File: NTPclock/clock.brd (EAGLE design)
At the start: 115 x 85 mm, 28 parts, among them IC1 MAX7219CNG

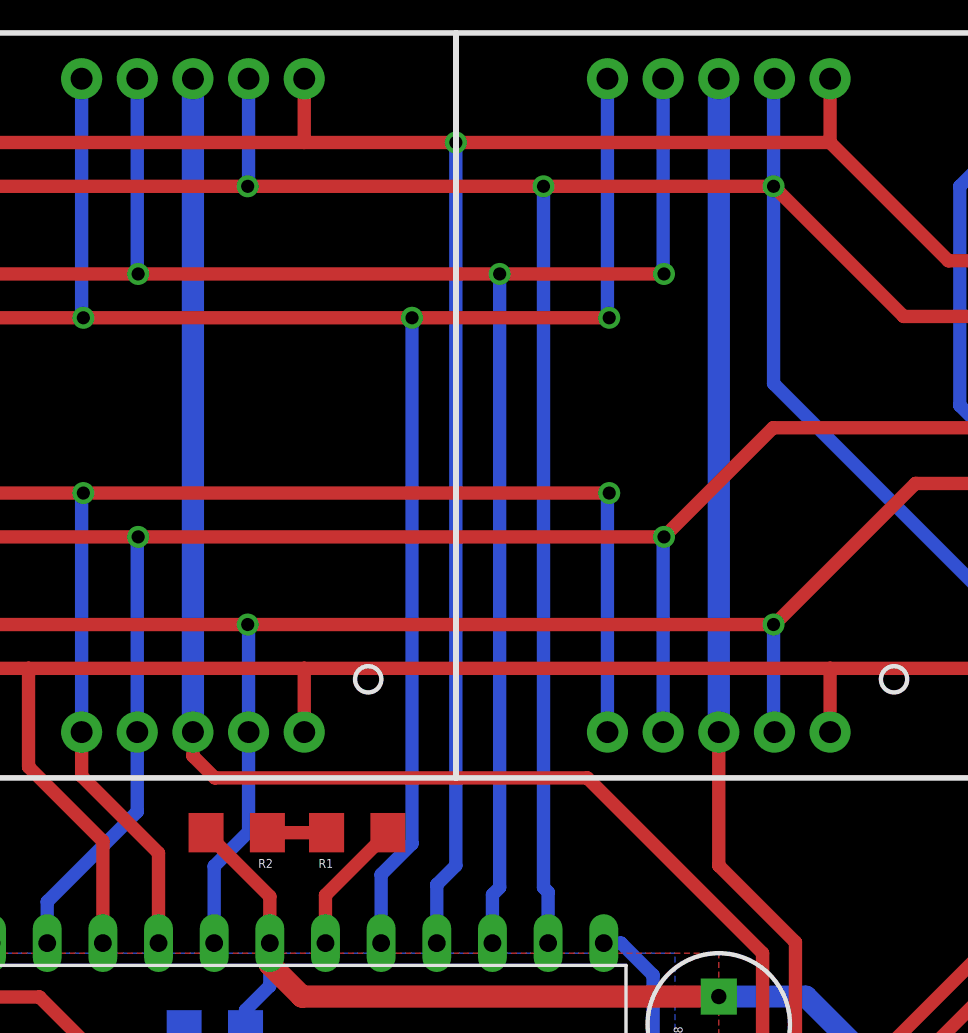
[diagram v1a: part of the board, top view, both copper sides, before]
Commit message: enable ground pour around lcds
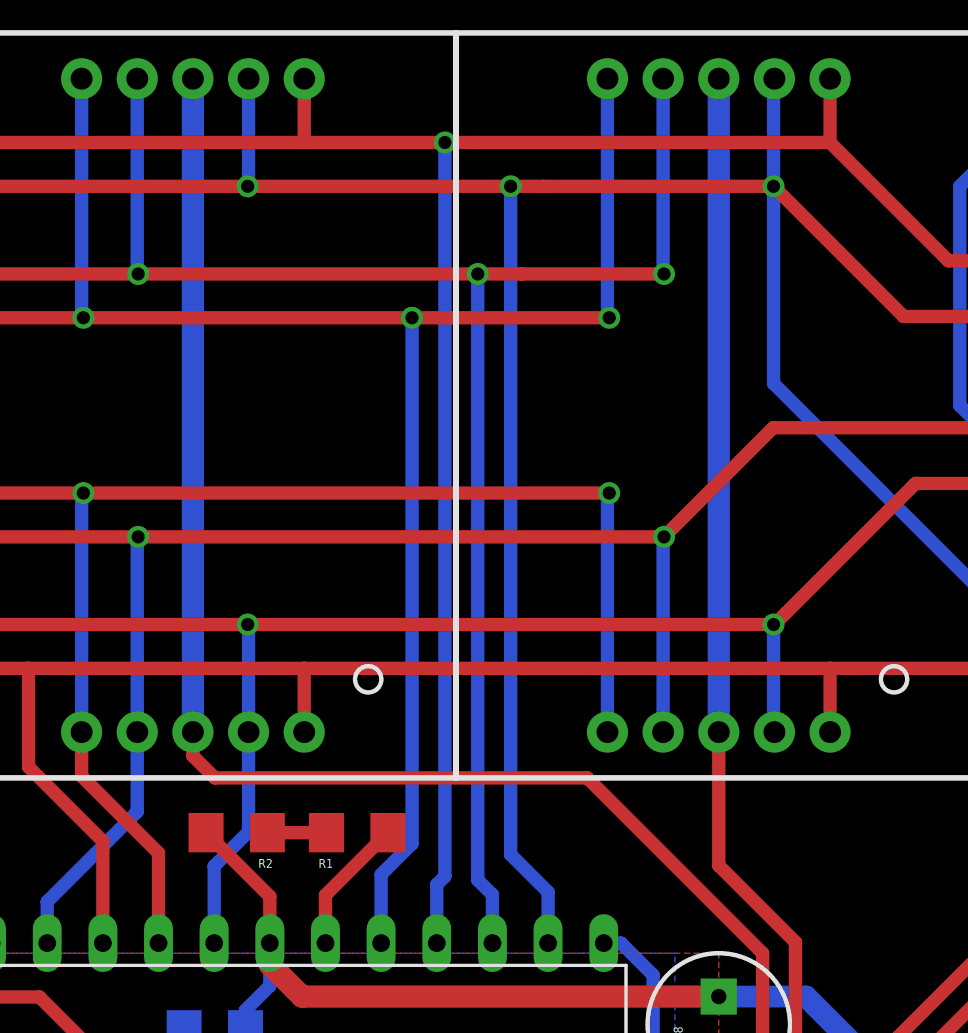
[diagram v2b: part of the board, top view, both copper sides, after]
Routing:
- net A: track 166.3 -> 166.9 mm
- removed copper zone on layer 1, net N$1
- removed copper zone on layer 16, net N$2
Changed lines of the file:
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@@
 <wire x1="91" y1="9.27" x2="60.13" y2="9.27" width="1" layer="1"/>
 <wire x1="60.13" y1="9.27" x2="60" y2="9.4" width="1" layer="1"/>
+<polygon width="0.6096" layer="16" isolate="0.6096">
+<vertex x="0" y="83"/>
+<vertex x="114" y="83"/>
+<vertex x="114" y="49"/>
+<vertex x="0" y="49"/>
+</polygon>
+<polygon width="0.6096" layer="1" isolate="0.6096">
+<vertex x="0" y="83"/>
+<vertex x="114" y="83"/>
+<vertex x="114" y="49"/>
+<vertex x="0" y="49"/>
+</polygon>
 </signal>
 <signal name="ISET">
@@
 <wire x1="19.45" y1="76" x2="38.5" y2="76" width="0.6096" layer="1"/>
 <wire x1="38.5" y1="76" x2="66.5" y2="76" width="0.6096" layer="1"/>
-<wire x1="66.5" y1="76" x2="80" y2="76" width="0.6096" layer="1"/>
+<wire x1="66.5" y1="76" x2="78.5" y2="76" width="0.6096" layer="1"/>
 <wire x1="80" y1="76" x2="90.5" y2="76" width="0.6096" layer="1"/>
 <wire x1="14.54" y1="80.91" x2="19.45" y2="76" width="0.6096" layer="1"/>
@@
 <via x="38.5" y="76" extent="1-16" drill="0.6" diameter="0.8"/>
 <wire x1="80.21" y1="41.46" x2="80.21" y2="43.79" width="0.6096" layer="16"/>
-<wire x1="80.21" y1="43.79" x2="80" y2="44" width="0.6096" layer="16"/>
-<wire x1="80" y1="44" x2="80" y2="76" width="0.6096" layer="16"/>
-<via x="80" y="76" extent="1-16" drill="0.6" diameter="0.8"/>
 <via x="90.5" y="76" extent="1-16" drill="0.6"/>
 <wire x1="90.5" y1="76" x2="90.5" y2="80.87" width="0.6096" layer="16"/>
@@
 <wire x1="102.19" y1="57.36" x2="100.14" y2="57.36" width="0.6096" layer="16"/>
 <wire x1="100.14" y1="57.36" x2="90.5" y2="67" width="0.6096" layer="16"/>
+<wire x1="80.21" y1="43.79" x2="78.5" y2="45.5" width="0.6096" layer="16"/>
+<wire x1="78.5" y1="45.5" x2="78.5" y2="76" width="0.6096" layer="16"/>
+<via x="78.5" y="76" extent="1-16" drill="0.6"/>
+<wire x1="78.5" y1="76" x2="80" y2="76" width="0.6096" layer="1"/>
 </signal>
 <signal name="B">
@@
 <wire x1="19.99" y1="78" x2="41.08" y2="78" width="0.6096" layer="1"/>
 <wire x1="41.08" y1="78" x2="69.08" y2="78" width="0.6096" layer="1"/>
-<wire x1="69.08" y1="78" x2="76" y2="78" width="0.6096" layer="1"/>
-<wire x1="76" y1="78" x2="93.08" y2="78" width="0.6096" layer="1"/>
+<wire x1="69.08" y1="78" x2="75.5" y2="78" width="0.6096" layer="1"/>
+<wire x1="77" y1="78" x2="93.08" y2="78" width="0.6096" layer="1"/>
 <wire x1="17.08" y1="80.91" x2="19.99" y2="78" width="0.6096" layer="1"/>
 <wire x1="41.08" y1="80.91" x2="41.08" y2="78" width="0.6096" layer="1"/>
@@
 <wire x1="93.08" y1="80.91" x2="93.08" y2="78" width="0.6096" layer="1"/>
 <wire x1="75.13" y1="41.46" x2="75.13" y2="44.13" width="0.6096" layer="16"/>
-<wire x1="75.13" y1="44.13" x2="76" y2="45" width="0.6096" layer="16"/>
-<wire x1="76" y1="45" x2="76" y2="78" width="0.6096" layer="16"/>
-<via x="76" y="78" extent="1-16" drill="0.6" diameter="0.8"/>
 <contactref element="BAR_GRAPH" pad="8"/>
 <contactref element="BAR_GRAPH" pad="3"/>
@@
 <wire x1="106" y1="62" x2="106" y2="71" width="0.6096" layer="1"/>
 <wire x1="106" y1="71" x2="104.4" y2="72.6" width="0.6096" layer="1"/>
+<wire x1="75.13" y1="44.13" x2="75.5" y2="44.5" width="0.6096" layer="16"/>
+<wire x1="75.5" y1="44.5" x2="75.5" y2="78" width="0.6096" layer="16"/>
+<via x="75.5" y="78" extent="1-16" drill="0.6"/>
+<wire x1="75.5" y1="78" x2="77" y2="78" width="0.6096" layer="1"/>
 </signal>
 <signal name="C">
@@
 <wire x1="33.5" y1="72" x2="48.73" y2="72" width="0.6096" layer="1"/>
 <wire x1="48.73" y1="72" x2="61.5" y2="72" width="0.6096" layer="1"/>
-<wire x1="61.5" y1="72" x2="78" y2="72" width="0.6096" layer="1"/>
-<wire x1="78" y1="72" x2="85.5" y2="72" width="0.6096" layer="1"/>
+<wire x1="61.5" y1="72" x2="77" y2="72" width="0.6096" layer="1"/>
+<wire x1="79" y1="72" x2="85.5" y2="72" width="0.6096" layer="1"/>
 <wire x1="85.46" y1="80.91" x2="85.46" y2="72" width="0.6096" layer="16"/>
 <wire x1="85.46" y1="72" x2="85.5" y2="72" width="0.6096" layer="16"/>
@@
 <wire x1="48.73" y1="74" x2="48.73" y2="72" width="0.6096" layer="1"/>
 <wire x1="77.67" y1="41.46" x2="77.67" y2="43.67" width="0.6096" layer="16"/>
-<wire x1="77.67" y1="43.67" x2="78" y2="44" width="0.6096" layer="16"/>
-<wire x1="78" y1="44" x2="78" y2="72" width="0.6096" layer="16"/>
-<via x="78" y="72" extent="1-16" drill="0.6" diameter="0.8"/>
+<wire x1="77.67" y1="43.67" x2="77" y2="44.34" width="0.6096" layer="16"/>
+<wire x1="77" y1="44.34" x2="77" y2="72" width="0.6096" layer="16"/>
+<via x="77" y="72" extent="1-16" drill="0.6"/>
+<wire x1="77" y1="72" x2="79" y2="72" width="0.6096" layer="1"/>
 </signal>
 <signal name="G">
@@
 <wire x1="20.6" y1="31" x2="16.4" y2="31" width="0.6096" layer="1"/>
 </signal>
-<signal name="N$1">
-<polygon width="0.6096" layer="1" pour="cutout">
-<vertex x="0" y="83"/>
-<vertex x="114" y="83"/>
-<vertex x="114" y="49"/>
-<vertex x="0" y="49"/>
-</polygon>
-</signal>
-<signal name="N$2">
-<polygon width="0.6096" layer="16" pour="cutout">
-<vertex x="0" y="83"/>
-<vertex x="114" y="83"/>
-<vertex x="114" y="49"/>
-<vertex x="0" y="49"/>
-</polygon>
-</signal>
 <signal name="N$3">

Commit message: Reorganize panel,
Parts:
- removed BUZ1: BUZZERPTH, SparkFun-Electromechanical:BUZZER-12MM
- removed J1: (no value), SparkFun-Connectors:1X02
- removed R4: 100Ω, SparkFun-Resistors:1206
- added BUTTONS: (no value), SparkFun-Connectors:MOLEX-1X6
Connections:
- removed net N$8: BUZ1.-, R4.1
- new net D3: BUTTONS.4, NODEMCU.V3.D3
- new net SD2: BUTTONS.5, NODEMCU.V3.SD2
- new net SD3: BUTTONS.6, NODEMCU.V3.SD3
- net D4: now also BUTTONS.3; no longer R4.2
- net D8: now also BUTTONS.2; no longer J1.1
- net GND: now also BUTTONS.1; no longer BUZ1.+, J1.2
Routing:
- net D3: track 0.00 -> 56.5 mm
- net SD2: track 0.00 -> 53.0 mm
- net SD3: track 0.00 -> 53.0 mm
- net GND: track 152.8 -> 121.3 mm
- net D8: track 23.2 -> 43.8 mm
- net D4: track 47.0 -> 56.5 mm
- net DIGIT7: track 63.8 -> 69.6 mm
- net N$8: track 5.43 -> 0.00 mm
- net DIGIT3: track 82.4 -> 85.6 mm
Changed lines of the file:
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@@
 <rectangle x1="31" y1="1" x2="49" y2="2" layer="41"/>
 <rectangle x1="31" y1="1" x2="49" y2="2" layer="42"/>
-<rectangle x1="31" y1="5" x2="32" y2="6" layer="42"/>
 <text x="55" y="-8" size="1.778" layer="48">Joshua villwock</text>
 <wire x1="115" y1="0" x2="115" y2="17" width="0" layer="20"/>
@@
 <text x="30.25" y="43" size="1.778" layer="21" rot="R270">RX
 TX</text>
+<rectangle x1="41" y1="24" x2="42" y2="25" layer="41"/>
 </plain>
 <attributes>
@@
 <attribute name="VALUE" x="51.905" y="56.349" size="1.27" layer="27" ratio="10"/>
 </element>
-<element name="BUZ1" library="SparkFun-Electromechanical" package="BUZZER-12MM" value="BUZZERPTH" x="70" y="21"/>
-<element name="J1" library="SparkFun-Connectors" package="1X02" value="" x="53" y="24"/>
-<element name="R4" library="SparkFun-Resistors" package="1206" value="100Ω" x="62" y="21.25" rot="R270"/>
 <element name="FRAME1" library="SparkFun-Aesthetics" package="CREATIVE_COMMONS" value="FRAME-LETTER" x="24" y="-8"/>
 <element name="SERIAL" library="SparkFun-Connectors" package="1X02" value="" x="33.75" y="37.75" rot="R180"/>
+<element name="BUTTONS" library="SparkFun-Connectors" package="MOLEX-1X6" value="" x="75" y="19" rot="MR0"/>
 </elements>
 <signals>
@@
 <wire x1="62.43" y1="35.43" x2="62.43" y2="33.84" width="1.016" layer="1"/>
 <wire x1="75.13" y1="33.84" x2="75.13" y2="36.48" width="1.016" layer="1"/>
-<wire x1="46" y1="9" x2="44" y2="7" width="0.6096" layer="1"/>
-<wire x1="44" y1="7" x2="41.25" y2="4.25" width="0.6096" layer="1"/>
-<wire x1="41.25" y1="4.25" x2="41.25" y2="3.13" width="0.6096" layer="1"/>
 <wire x1="23.47" y1="25.99" x2="23.4" y2="26.06" width="0.6096" layer="1"/>
 <wire x1="23.4" y1="26.06" x2="23.4" y2="31" width="0.6096" layer="1"/>
@@
 <vertex x="-2" y="87"/>
 </polygon>
-<wire x1="31.09" y1="3.13" x2="31.09" y2="5" width="0.6096" layer="1"/>
-<wire x1="31.09" y1="5" x2="31.09" y2="5.09" width="0.6096" layer="1"/>
-<wire x1="31.09" y1="5.09" x2="33" y2="7" width="0.6096" layer="1"/>
-<wire x1="33" y1="7" x2="44" y2="7" width="0.6096" layer="1"/>
-<wire x1="10.77" y1="3.13" x2="10.77" y2="4.27" width="0.6096" layer="1"/>
-<wire x1="11.5" y1="5" x2="31.09" y2="5" width="0.6096" layer="1"/>
-<wire x1="10.77" y1="4.27" x2="11.5" y2="5" width="0.6096" layer="1"/>
-<contactref element="J1" pad="2"/>
-<contactref element="BUZ1" pad="+"/>
 <wire x1="63.6" y1="37.5" x2="63.6" y2="36.6" width="0.6096" layer="16"/>
 <wire x1="63.6" y1="36.6" x2="62.43" y2="35.43" width="0.6096" layer="16"/>
@@
 <wire x1="60" y1="9.4" x2="54.63" y2="9.4" width="1" layer="1"/>
 <wire x1="54.63" y1="9.4" x2="54.5" y2="9.27" width="1" layer="1"/>
-<wire x1="46" y1="9" x2="54.23" y2="9" width="0.6096" layer="1"/>
-<wire x1="54.23" y1="9" x2="54.5" y2="9.27" width="0.6096" layer="1"/>
 <wire x1="91" y1="9.27" x2="60.13" y2="9.27" width="1" layer="1"/>
 <wire x1="60.13" y1="9.27" x2="60" y2="9.4" width="1" layer="1"/>
-<polygon width="0.6096" layer="16" isolate="0.6096">
-<vertex x="0" y="83"/>
-<vertex x="114" y="83"/>
-<vertex x="114" y="49"/>
-<vertex x="0" y="49"/>
-</polygon>
-<polygon width="0.6096" layer="1" isolate="0.6096">
-<vertex x="0" y="83"/>
-<vertex x="114" y="83"/>
-<vertex x="114" y="49"/>
-<vertex x="0" y="49"/>
-</polygon>
+<contactref element="BUTTONS" pad="1"/>
+<wire x1="10.77" y1="3.13" x2="12.64" y2="5" width="0.6096" layer="16"/>
+<wire x1="12.64" y1="5" x2="30" y2="5" width="0.6096" layer="16"/>
+<wire x1="30" y1="5" x2="31.09" y2="3.91" width="0.6096" layer="16"/>
+<wire x1="31.09" y1="3.91" x2="31.09" y2="3.13" width="0.6096" layer="16"/>
 </signal>
 <signal name="ISET">
@@
 <wire x1="76" y1="30" x2="79" y2="27" width="0.6096" layer="1"/>
 <wire x1="79" y1="27" x2="88" y2="27" width="0.6096" layer="1"/>
-<wire x1="88" y1="27" x2="107.5" y2="46.5" width="0.6096" layer="1"/>
-<wire x1="107.5" y1="66.5" x2="107.5" y2="46.5" width="0.6096" layer="1"/>
+<wire x1="107.5" y1="66.5" x2="107.5" y2="54" width="0.6096" layer="1"/>
+<wire x1="88" y1="27" x2="94.5" y2="33.5" width="0.6096" layer="1"/>
+<wire x1="94.5" y1="33.5" x2="94.5" y2="46.5" width="0.6096" layer="1"/>
+<wire x1="94.5" y1="46.5" x2="98.5" y2="50.5" width="0.6096" layer="1"/>
+<wire x1="98.5" y1="50.5" x2="104" y2="50.5" width="0.6096" layer="1"/>
+<wire x1="104" y1="50.5" x2="107.5" y2="54" width="0.6096" layer="1"/>
 </signal>
 <signal name="A">
@@
 <wire x1="76.5" y1="31.5" x2="79.5" y2="28.5" width="0.6096" layer="1"/>
 <wire x1="79.5" y1="28.5" x2="87.5" y2="28.5" width="0.6096" layer="1"/>
-<wire x1="87.5" y1="28.5" x2="105" y2="46" width="0.6096" layer="1"/>
-<via x="105" y="46" extent="1-16" drill="0.6" diameter="0.8"/>
-<wire x1="105" y1="46" x2="109.81" y2="50.81" width="0.6096" layer="16"/>
-<wire x1="109.81" y1="50.81" x2="109.81" y2="54.82" width="0.6096" layer="16"/>
+<wire x1="109.81" y1="54" x2="109.81" y2="54.82" width="0.6096" layer="16"/>
+<wire x1="87.5" y1="28.5" x2="93" y2="34" width="0.6096" layer="1"/>
+<wire x1="93" y1="34" x2="93" y2="47" width="0.6096" layer="1"/>
+<wire x1="93" y1="47" x2="98" y2="52" width="0.6096" layer="1"/>
+<wire x1="103" y1="52" x2="107.81" y2="52" width="0.6096" layer="16"/>
+<wire x1="107.81" y1="52" x2="109.81" y2="54" width="0.6096" layer="16"/>
+<wire x1="98" y1="52" x2="103" y2="52" width="0.6096" layer="1"/>
+<via x="103" y="52" extent="1-16" drill="0.6" diameter="0.8128"/>
 </signal>
 <signal name="DIGIT6">
@@
 <polygon width="0.6096" layer="16" pour="cutout">
 <vertex x="0" y="28"/>
-<vertex x="30" y="28"/>
-<vertex x="30" y="0"/>
+<vertex x="27" y="28"/>
+<vertex x="27" y="0"/>
 <vertex x="0" y="0"/>
 </polygon>
@@
 <polygon width="0.6096" layer="1" pour="cutout">
 <vertex x="0" y="28"/>
-<vertex x="30" y="28"/>
-<vertex x="30" y="0"/>
+<vertex x="27" y="28"/>
+<vertex x="27" y="0"/>
 <vertex x="0" y="0"/>
 </polygon>
@@
 <signal name="D4">
 <contactref element="NODEMCU.V3" pad="D4"/>
-<contactref element="R4" pad="2"/>
-<wire x1="18.39" y1="25.99" x2="18.39" y2="24.61" width="0.6096" layer="1"/>
-<wire x1="18.39" y1="24.61" x2="23" y2="20" width="0.6096" layer="1"/>
-<wire x1="23" y1="20" x2="61.85" y2="20" width="0.6096" layer="1"/>
-<wire x1="61.85" y1="20" x2="62" y2="19.85" width="0.6096" layer="1"/>
+<contactref element="BUTTONS" pad="3"/>
+<wire x1="18.39" y1="25.99" x2="24.38" y2="20" width="0.6096" layer="1"/>
+<wire x1="58" y1="20" x2="60.5" y2="22.5" width="0.6096" layer="1"/>
+<wire x1="60.5" y1="22.5" x2="66.42" y2="22.5" width="0.6096" layer="1"/>
+<wire x1="66.42" y1="22.5" x2="69.92" y2="19" width="0.6096" layer="1"/>
+<wire x1="24.38" y1="20" x2="58" y2="20" width="0.6096" layer="1"/>
 </signal>
 <signal name="D8">
 <contactref element="NODEMCU.V3" pad="D8"/>
-<contactref element="J1" pad="1"/>
-<wire x1="36.5" y1="21.5" x2="33.63" y2="24.37" width="0.6096" layer="1"/>
-<wire x1="33.63" y1="24.37" x2="33.63" y2="25.99" width="0.6096" layer="1"/>
-<wire x1="53" y1="24" x2="50.5" y2="21.5" width="0.6096" layer="1"/>
-<wire x1="50.5" y1="21.5" x2="36.5" y2="21.5" width="0.6096" layer="1"/>
-</signal>
-<signal name="N$8">
-<contactref element="R4" pad="1"/>
-<contactref element="BUZ1" pad="-"/>
-<wire x1="62" y1="22.65" x2="65.1" y2="22.65" width="0.6096" layer="1"/>
-<wire x1="65.1" y1="22.65" x2="66.75" y2="21" width="0.6096" layer="1"/>
+<contactref element="BUTTONS" pad="2"/>
+<wire x1="33.63" y1="25.99" x2="38.12" y2="21.5" width="0.6096" layer="1"/>
+<wire x1="57.5" y1="21.5" x2="60" y2="24" width="0.6096" layer="1"/>
+<wire x1="60" y1="24" x2="67.46" y2="24" width="0.6096" layer="1"/>
+<wire x1="67.46" y1="24" x2="72.46" y2="19" width="0.6096" layer="1"/>
+<wire x1="38.12" y1="21.5" x2="57.5" y2="21.5" width="0.6096" layer="1"/>
 </signal>
 <signal name="RX">
 <contactref element="NODEMCU.V3" pad="RX"/>
 <contactref element="SERIAL" pad="2"/>
-<wire x1="36.17" y1="25.99" x2="36.17" y2="29.83" width="0.4064" layer="1"/>
-<wire x1="36.17" y1="29.83" x2="31.21" y2="34.79" width="0.4064" layer="1"/>
-<wire x1="31.21" y1="34.79" x2="31.21" y2="37.75" width="0.4064" layer="1"/>
+<wire x1="36.17" y1="25.99" x2="36.17" y2="32.79" width="0.6096" layer="1"/>
+<wire x1="36.17" y1="32.79" x2="31.21" y2="37.75" width="0.6096" layer="1"/>
 </signal>
 <signal name="TX">
 <contactref element="NODEMCU.V3" pad="TX"/>
 <contactref element="SERIAL" pad="1"/>
-<wire x1="38.71" y1="25.99" x2="38.71" y2="29.29" width="0.4064" layer="1"/>
-<wire x1="38.71" y1="29.29" x2="33.75" y2="34.25" width="0.4064" layer="1"/>
-<wire x1="33.75" y1="34.25" x2="33.75" y2="37.75" width="0.4064" layer="1"/>
+<wire x1="33.75" y1="37.75" x2="37.75" y2="33.75" width="0.6096" layer="1"/>
+<wire x1="37.75" y1="33.75" x2="37.75" y2="26.95" width="0.6096" layer="1"/>
+<wire x1="37.75" y1="26.95" x2="38.71" y2="25.99" width="0.6096" layer="1"/>
+</signal>
+<signal name="D3">
+<contactref element="NODEMCU.V3" pad="D3"/>
+<contactref element="BUTTONS" pad="4"/>
+<wire x1="15.85" y1="25.99" x2="23.34" y2="18.5" width="0.6096" layer="1"/>
+<wire x1="58.5" y1="18.5" x2="61" y2="21" width="0.6096" layer="1"/>
+<wire x1="67.38" y1="19" x2="65.38" y2="21" width="0.6096" layer="1"/>
+<wire x1="65.38" y1="21" x2="61" y2="21" width="0.6096" layer="1"/>
+<wire x1="23.34" y1="18.5" x2="58.5" y2="18.5" width="0.6096" layer="1"/>
+</signal>
+<signal name="SD2">
+<contactref element="NODEMCU.V3" pad="SD2"/>
+<contactref element="BUTTONS" pad="5"/>
+<wire x1="61.34" y1="15.5" x2="64.84" y2="19" width="0.6096" layer="1"/>
+<wire x1="18.39" y1="3.13" x2="30.76" y2="15.5" width="0.6096" layer="1"/>
+<wire x1="30.76" y1="15.5" x2="61.34" y2="15.5" width="0.6096" layer="1"/>
+</signal>
+<signal name="SD3">
+<contactref element="NODEMCU.V3" pad="SD3"/>
+<contactref element="BUTTONS" pad="6"/>
+<wire x1="60.3" y1="17" x2="62.3" y2="19" width="0.6096" layer="1"/>
+<wire x1="15.85" y1="3.13" x2="29.72" y2="17" width="0.6096" layer="1"/>
+<wire x1="29.72" y1="17" x2="60.3" y2="17" width="0.6096" layer="1"/>
 </signal>
 </signals>
